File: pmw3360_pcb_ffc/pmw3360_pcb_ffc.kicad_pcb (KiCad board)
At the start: 2 copper layers, 27 x 22.5 mm, 20 parts, among them J1 Interface, U1 PMW3360DM-T2QU, U2 TPS73601DBV

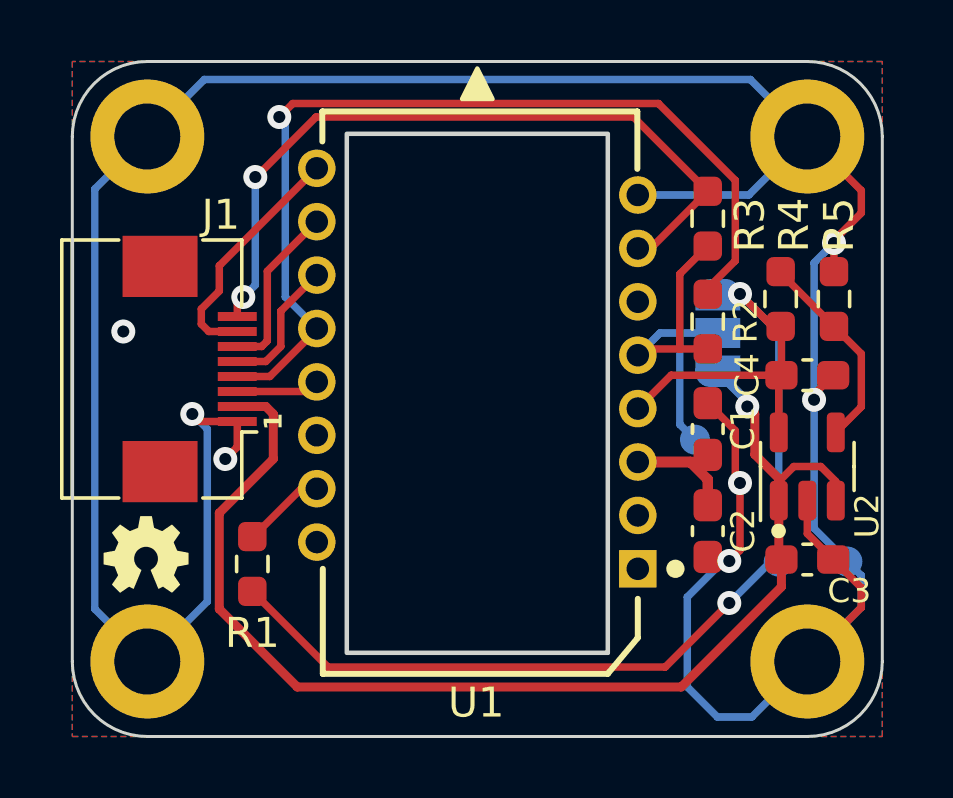
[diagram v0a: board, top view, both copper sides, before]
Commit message: Update symbol references
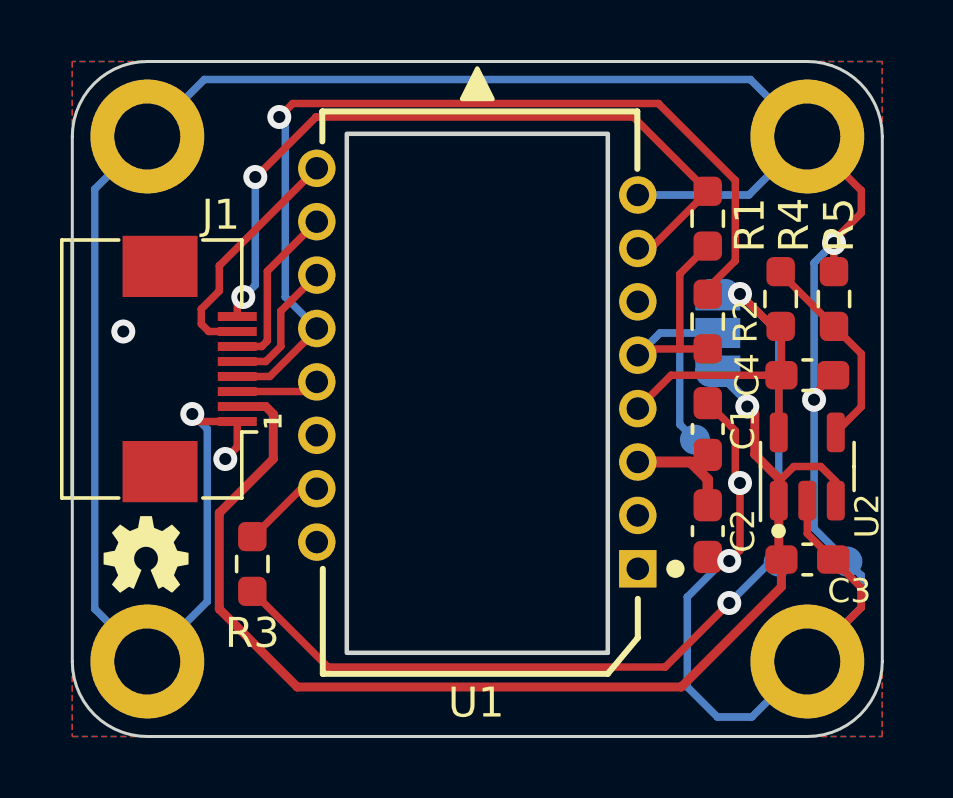
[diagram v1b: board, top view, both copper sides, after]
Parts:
- renumbered R3 to R1, R1 to R3
